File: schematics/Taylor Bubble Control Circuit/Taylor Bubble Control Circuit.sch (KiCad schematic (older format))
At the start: 13 parts, among them J1 Conn_01x01, J2 Conn_01x02, J3 Conn_01x03, U1 L7805CV-DG, U1 STM32F446RE Board, U2 TL062

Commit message: schematics edited
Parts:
- C3, C4: renamed from C?; value C -> 100n
- gave numbers to parts that had none: 2
- renumbered U1 to U2, U2 to U3
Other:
- note added: "3.3V to 4.95V conversion"
- note added: "8... 12 V Voltage Supply Connector\n"
- note added: "ADC input"
- note added: "Transimpedance amplifier"
- note added: "close to U3"
- note removed: "8... 12 V Voltage Supply Input\n"
- note removed: "Analog In"
- note removed: "close to V+"
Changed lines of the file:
@@
 encoding utf-8
 Sheet 1 1
-Title ""
-Date ""
-Rev ""
-Comp ""
+Title "Taylor Bubble Control Circuit"
+Date "2022-07-07"
+Rev "1.0"
+Comp "TU Dresden"
 Comment1 ""
 Comment2 ""
@@
 $EndDescr
 $Comp
-L Amplifier_Operational:TL062 U2
+L Amplifier_Operational:TL062 U3
 U 1 1 62CD608B
 P 2950 2550
-F 0 "U2" H 2950 2917 50  0000 C CNN
+F 0 "U3" H 2950 2917 50  0000 C CNN
 F 1 "TL062" H 2950 2826 50  0000 C CNN
 F 2 "" H 2950 2550 50  0001 C CNN
@@
 $EndComp
 $Comp
-L Amplifier_Operational:TL062 U2
+L Amplifier_Operational:TL062 U3
 U 3 1 62CDCC37
 P 5650 1650
-F 0 "U2" H 5608 1696 50  0000 L CNN
+F 0 "U3" H 5608 1696 50  0000 L CNN
 F 1 "TL062" H 5608 1605 50  0000 L CNN
 F 2 "" H 5650 1650 50  0001 C CNN
@@
 $EndComp
 $Comp
-L Device:R_POT RV?
+L Device:R_POT RV1
 U 1 1 62CF5B88
 P 3450 2800
-F 0 "RV?" V 3335 2800 50  0000 C CNN
+F 0 "RV1" V 3335 2800 50  0000 C CNN
 F 1 "R_POT" V 3244 2800 50  0000 C CNN
 F 2 "" H 3450 2800 50  0001 C CNN
@@
 	2650 2800 2650 2650
 $Comp
-L power:GND #PWR?
+L power:GND #PWR01
 U 1 1 62CF9495
 P 2500 2450
-F 0 "#PWR?" H 2500 2200 50  0001 C CNN
+F 0 "#PWR01" H 2500 2200 50  0001 C CNN
 F 1 "GND" H 2505 2277 50  0000 C CNN
 F 2 "" H 2500 2450 50  0001 C CNN
@@
 	2650 2800 3300 2800
 $Comp
-L power:GND #PWR?
+L power:GND #PWR03
 U 1 1 62D170A5
 P 2650 2900
-F 0 "#PWR?" H 2650 2650 50  0001 C CNN
+F 0 "#PWR03" H 2650 2650 50  0001 C CNN
 F 1 "GND" H 2655 2727 50  0000 C CNN
 F 2 "" H 2650 2900 50  0001 C CNN
@@
 $EndComp
 $Comp
-L Regulator_Linear:L7805 U1
+L Regulator_Linear:L7805 U2
 U 1 1 62D18C8D
 P 3350 1350
-F 0 "U1" H 3350 1592 50  0000 C CNN
+F 0 "U2" H 3350 1592 50  0000 C CNN
 F 1 "L7805CV-DG" H 3350 1501 50  0000 C CNN
 F 2 "" H 3375 1200 50  0001 L CIN
@@
 $EndComp
 $Comp
-L Device:CP C?
+L Device:CP C2
 U 1 1 62D1B42A
 P 3750 1500
-F 0 "C?" H 3868 1546 50  0000 L CNN
+F 0 "C2" H 3868 1546 50  0000 L CNN
 F 1 "330n" H 3868 1455 50  0000 L CNN
 F 2 "" H 3788 1350 50  0001 C CNN
@@
 	3050 1350 2750 1350
 $Comp
-L power:GND #PWR?
+L power:GND #PWR04
 U 1 1 62D1D949
 P 2750 1650
-F 0 "#PWR?" H 2750 1400 50  0001 C CNN
+F 0 "#PWR04" H 2750 1400 50  0001 C CNN
 F 1 "GND" H 2755 1477 50  0000 C CNN
 F 2 "" H 2750 1650 50  0001 C CNN
@@
 $EndComp
 $Comp
-L power:GND #PWR?
+L power:GND #PWR06
 U 1 1 62D1DB97
 P 3750 1650
-F 0 "#PWR?" H 3750 1400 50  0001 C CNN
+F 0 "#PWR06" H 3750 1400 50  0001 C CNN
 F 1 "GND" H 3755 1477 50  0000 C CNN
 F 2 "" H 3750 1650 50  0001 C CNN
@@
 $EndComp
 $Comp
-L power:GND #PWR?
+L power:GND #PWR05
 U 1 1 62D1E0D5
 P 3350 1650
-F 0 "#PWR?" H 3350 1400 50  0001 C CNN
+F 0 "#PWR05" H 3350 1400 50  0001 C CNN
 F 1 "GND" H 3355 1477 50  0000 C CNN
 F 2 "" H 3350 1650 50  0001 C CNN
@@
 Connection ~ 2750 1350
 $Comp
-L power:GND #PWR?
+L power:GND #PWR010
 U 1 1 62D27363
 P 5550 1950
-F 0 "#PWR?" H 5550 1700 50  0001 C CNN
+F 0 "#PWR010" H 5550 1700 50  0001 C CNN
 F 1 "GND" H 5555 1777 50  0000 C CNN
 F 2 "" H 5550 1950 50  0001 C CNN
@@
 close to U1
 $Comp
-L Device:C C?
+L Device:C C4
 U 1 1 62D4D672
 P 5150 1500
-F 0 "C?" H 5035 1454 50  0000 R CNN
-F 1 "C" H 5035 1545 50  0000 R CNN
+F 0 "C4" H 5035 1454 50  0000 R CNN
+F 1 "100n" H 5035 1545 50  0000 R CNN
 F 2 "" H 5188 1350 50  0001 C CNN
 F 3 "~" H 5150 1500 50  0001 C CNN
@@
 $EndComp
 $Comp
-L power:GND #PWR?
+L power:GND #PWR09
 U 1 1 62D4E897
 P 5150 1650
-F 0 "#PWR?" H 5150 1400 50  0001 C CNN
+F 0 "#PWR09" H 5150 1400 50  0001 C CNN
 F 1 "GND" H 5155 1477 50  0000 C CNN
 F 2 "" H 5150 1650 50  0001 C CNN
@@
 $EndComp
 Text Notes 4950 1650 0    50   ~ 0
-close to V+
+close to U3
 Wire Wire Line
 	5150 1350 5550 1350
@@
 	3950 3900 4100 3900
 $Comp
-L power:GND #PWR?
+L power:GND #PWR07
 U 1 1 62DDF2C7
 P 4100 4200
-F 0 "#PWR?" H 4100 3950 50  0001 C CNN
+F 0 "#PWR07" H 4100 3950 50  0001 C CNN
 F 1 "GND" H 4105 4027 50  0000 C CNN
 F 2 "" H 4100 4200 50  0001 C CNN
@@
 $EndComp
 $Comp
-L Device:C C?
+L Device:C C3
 U 1 1 62DDF2C1
 P 4100 4050
-F 0 "C?" H 3985 4004 50  0000 R CNN
-F 1 "C" H 3985 4095 50  0000 R CNN
+F 0 "C3" H 3985 4004 50  0000 R CNN
+F 1 "100n" H 3985 4095 50  0000 R CNN
 F 2 "" H 4138 3900 50  0001 C CNN
 F 3 "~" H 4100 4050 50  0001 C CNN
@@
 	2600 3900 2600 4100
 $Comp
-L Amplifier_Operational:TL062 U2
+L Amplifier_Operational:TL062 U3
 U 2 1 62CE49AF
 P 2900 3800
-F 0 "U2" H 2900 4167 50  0000 C CNN
+F 0 "U3" H 2900 4167 50  0000 C CNN
 F 1 "TL062" H 2900 4076 50  0000 C CNN
 F 2 "" H 2900 3800 50  0001 C CNN
@@
 	3200 4100 2600 4100
 $Comp
-L power:GND #PWR?
+L power:GND #PWR02
 U 1 1 62D6259C
 P 2600 4500
-F 0 "#PWR?" H 2600 4250 50  0001 C CNN
+F 0 "#PWR02" H 2600 4250 50  0001 C CNN
 F 1 "GND" H 2605 4327 50  0000 C CNN
 F 2 "" H 2600 4500 50  0001 C CNN
@@
 Servo Motor Connectors
 $Comp
-L power:GND #PWR?
+L power:GND #PWR08
 U 1 1 62DDD2CF
 P 4600 4000
-F 0 "#PWR?" H 4600 3750 50  0001 C CNN
+F 0 "#PWR08" H 4600 3750 50  0001 C CNN
 F 1 "GND" H 4605 3827 50  0000 C CNN
 F 2 "" H 4600 4000 50  0001 C CNN
@@
 Wire Notes Line
 	1400 1500 1400 1200
-Text Notes 1250 1150 0    50   ~ 0
-8... 12 V Voltage Supply Input\n
 Wire Wire Line
 	1950 2800 2650 2800
@@
 PWM_3v3
 Text Notes 9400 1550 0    50   ~ 0
-Analog In
+ADC input
 Text GLabel 9850 1550 2    50   Input ~ 0
 PhotoVoltage
@@
 	8650 4850 8650 4800
 $Comp
-L power:GND #PWR?
+L power:GND #PWR011
 U 1 1 62D8D228
 P 8650 4850
-F 0 "#PWR?" H 8650 4600 50  0001 C CNN
+F 0 "#PWR011" H 8650 4600 50  0001 C CNN
 F 1 "GND" H 8650 4700 50  0000 C CNN
 F 2 "" H 8650 4850 50  0001 C CNN
@@
 NoConn ~ 9350 1750
 NoConn ~ 9350 1850
+Text Notes 2550 1650 0    50   ~ 0
+close to U1
+Text Notes 2550 2100 0    50   ~ 0
+Transimpedance amplifier
+Text Notes 2500 3350 0    50   ~ 0
+3.3V to 4.95V conversion
+Text Notes 1250 1150 0    50   ~ 0
+8... 12 V Voltage Supply Connector\n
 $EndSCHEMATC

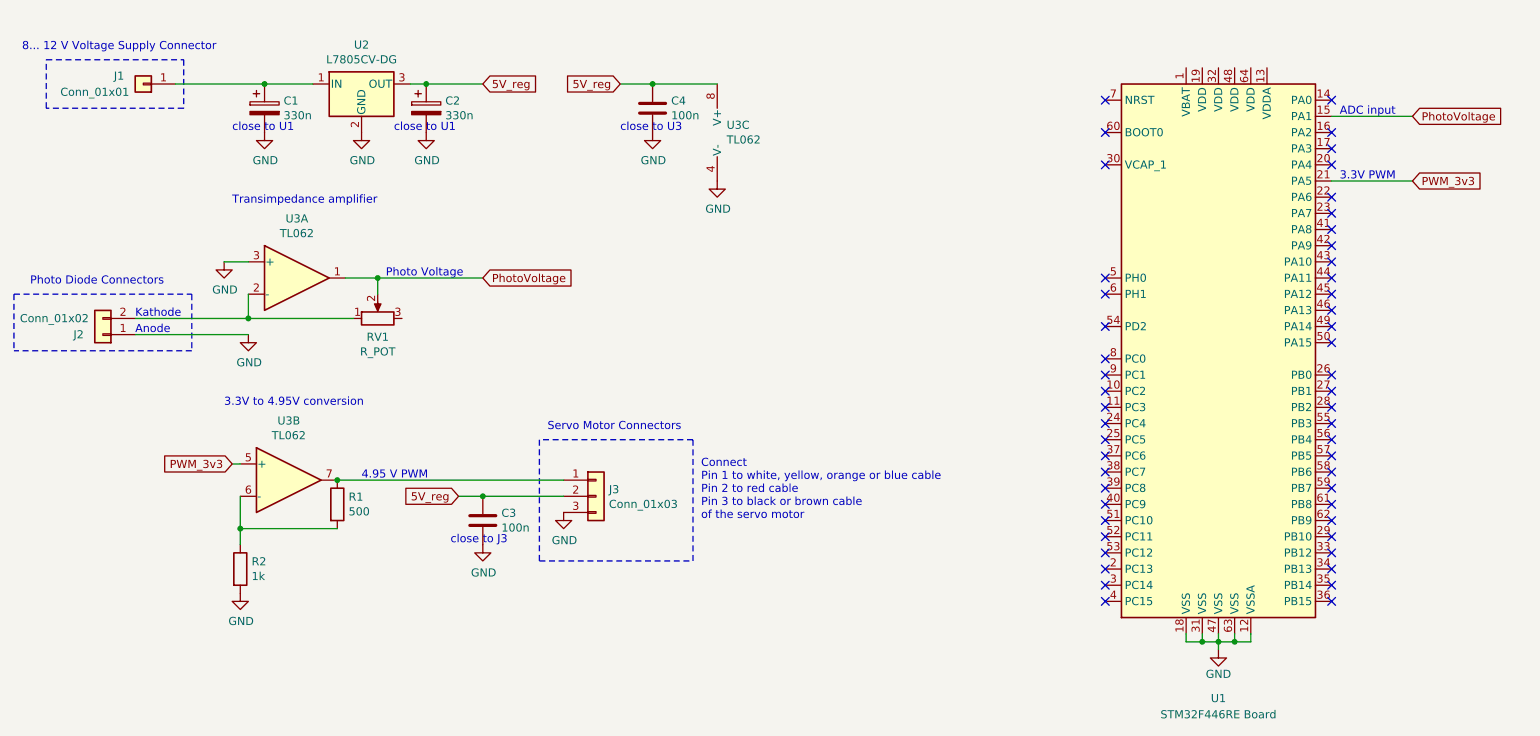
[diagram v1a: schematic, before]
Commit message: updated schematics
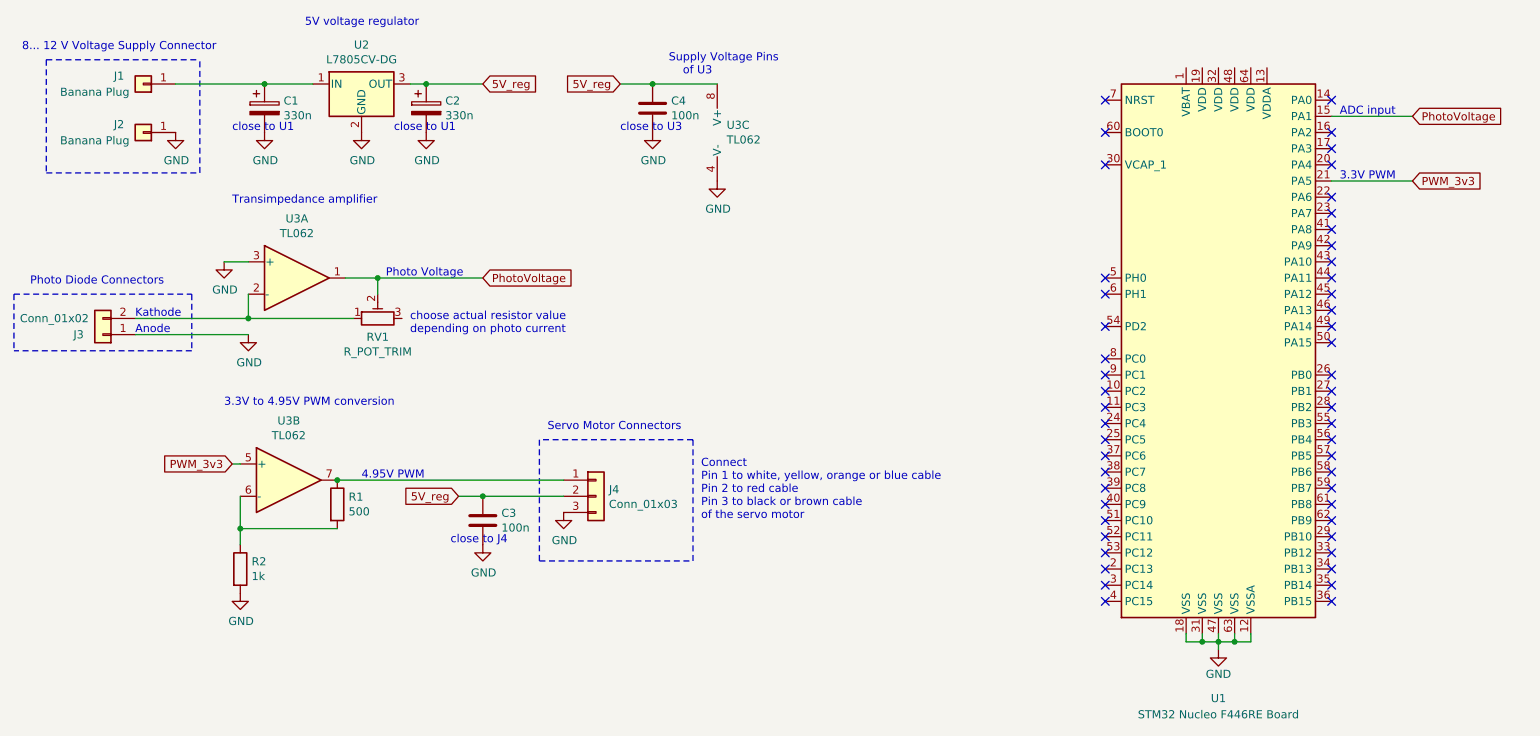
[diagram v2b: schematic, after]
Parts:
- removed RV1: R_POT, symbol Device:R_POT
- added J2: Banana Plug, symbol Connector_Generic:Conn_01x01
- added RV1: R_POT_TRIM, symbol Device:R_POT_TRIM
- C1, C2: Reichelt link (none) -> https://www.reichelt.de/subminiatur-elko-radial-330-nf-63-v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
- C3, C4: Reichelt link (none) -> https://www.reichelt.de/keramik-kondensator-100-nf-20-80-y5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
- J1: value Conn_01x01 -> Banana Plug; Reichelt link (none) -> https://www.reichelt.de/bananenbuchse-4mm-vollisoliert-rot-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
- J3: renamed from J2; Reichelt link (none) -> https://www.reichelt.de/fahrstuhlklemme-2-pol-4-mm-rm-5-08-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
- J4: renamed from J3; Reichelt link (none) -> https://www.reichelt.de/fahrstuhlklemme-3-pol-4-mm-rm-5-08-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
- U1: value STM32F446RE Board -> STM32 Nucleo F446RE Board; Reichelt link (none) -> https://www.reichelt.de/nucleo-64-arm-cortex-stm32-f446-ser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
- U2: Reichelt link (none) -> https://www.reichelt.de/spannungsregler-fest-5-v-1-5a-4-to-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
- U3: Reichelt link (none) -> https://www.reichelt.de/operationsverstaerker-2-fach-dip-8-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
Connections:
- net GND: now also J2.1 (Pin_1)
- net PhotoVoltage: now also RV1.2
- net at J3.2 (Pin_2), U3.2 (-): now also RV1.1
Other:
- note added: "3.3V to 4.95V PWM conversion"
- note added: "4.95V PWM"
- note added: "5V voltage regulator"
- note added: "Supply Voltage Pins \n of U3"
- note added: "choose actual resistor value \ndepending on photo current"
- note added: "close to J4"
- note removed: "3.3V to 4.95V conversion"
- note removed: "4.95 V PWM"
- note removed: "close to J3"
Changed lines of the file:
@@
 F 1 "TL062" H 2950 2826 50  0000 C CNN
 F 2 "" H 2950 2550 50  0001 C CNN
-F 3 "http://www.ti.com/lit/ds/symlink/tl061.pdf" H 2950 2550 50  0001 C CNN
+F 3 "https://www.reichelt.de/index.html?ACTION=7&LA=3&OPEN=0&INDEX=0&FILENAME=A200%2FTL062%23STM.pdf" H 2950 2550 50  0001 C CNN
+F 4 "https://www.reichelt.de/operationsverstaerker-2-fach-dip-8-tl-062-dip-p21552.html?&GROUP=A2C4&START=0&SORT=preis&OFFSET=16&nbc=1" H 2950 2550 50  0001 C CNN "Reichelt link"
 	1    2950 2550
 	1    0    0    -1
@@
 F 1 "TL062" H 5608 1605 50  0000 L CNN
 F 2 "" H 5650 1650 50  0001 C CNN
-F 3 "http://www.ti.com/lit/ds/symlink/tl061.pdf" H 5650 1650 50  0001 C CNN
+F 3 "https://www.reichelt.de/index.html?ACTION=7&LA=3&OPEN=0&INDEX=0&FILENAME=A200%2FTL062%23STM.pdf" H 5650 1650 50  0001 C CNN
+F 4 "https://www.reichelt.de/operationsverstaerker-2-fach-dip-8-tl-062-dip-p21552.html?&GROUP=A2C4&START=0&SORT=preis&OFFSET=16&nbc=1" H 5650 1650 50  0001 C CNN "Reichelt link"
 	3    5650 1650
 	1    0    0    -1
-$EndComp
-$Comp
-L Device:R_POT RV1
-U 1 1 62CF5B88
-P 3450 2800
-F 0 "RV1" V 3335 2800 50  0000 C CNN
-F 1 "R_POT" V 3244 2800 50  0000 C CNN
-F 2 "" H 3450 2800 50  0001 C CNN
-F 3 "~" H 3450 2800 50  0001 C CNN
-	1    3450 2800
-	0    -1   -1   0
 $EndComp
 Wire Wire Line
@@
 F 1 "L7805CV-DG" H 3350 1501 50  0000 C CNN
 F 2 "" H 3375 1200 50  0001 L CIN
-F 3 "http://www.st.com/content/ccc/resource/technical/document/datasheet/41/4f/b3/b0/12/d4/47/88/CD00000444.pdf/files/CD00000444.pdf/jcr:content/translations/en.CD00000444.pdf" H 3350 1300 50  0001 C CNN
+F 3 "https://www.reichelt.de/index.html?ACTION=7&LA=3&OPEN=0&INDEX=0&FILENAME=A200%2FL78_ENG_TDS.pdf" H 3350 1300 50  0001 C CNN
+F 4 "https://www.reichelt.de/spannungsregler-fest-5-v-1-5a-4-to-220-l7805cv-dg-stm-p216677.html?&GROUP=A2A2&START=0&SORT=preis&OFFSET=16&nbc=1" H 3350 1350 50  0001 C CNN "Reichelt link"
 	1    3350 1350
 	1    0    0    -1
@@
 F 1 "330n" H 2868 1455 50  0000 L CNN
 F 2 "" H 2788 1350 50  0001 C CNN
-F 3 "~" H 2750 1500 50  0001 C CNN
+F 3 "https://www.reichelt.de/index.html?ACTION=7&LA=3&OPEN=0&INDEX=0&FILENAME=B300%2FSM_TRANS.pdf" H 2750 1500 50  0001 C CNN
+F 4 "https://www.reichelt.de/subminiatur-elko-radial-330-nf-63-v-rm-1-5-85-c-1000h-20--sm-0-33-63rad-p18159.html?&GROUP=B315&START=0&SORT=preis&OFFSET=16&nbc=1" H 2750 1500 50  0001 C CNN "Reichelt link"
 	1    2750 1500
 	1    0    0    -1
@@
 F 1 "330n" H 3868 1455 50  0000 L CNN
 F 2 "" H 3788 1350 50  0001 C CNN
-F 3 "~" H 3750 1500 50  0001 C CNN
+F 3 "https://www.reichelt.de/index.html?ACTION=7&LA=3&OPEN=0&INDEX=0&FILENAME=B300%2FSM_TRANS.pdf" H 3750 1500 50  0001 C CNN
+F 4 "https://www.reichelt.de/subminiatur-elko-radial-330-nf-63-v-rm-1-5-85-c-1000h-20--sm-0-33-63rad-p18159.html?&GROUP=B315&START=0&SORT=preis&OFFSET=16&nbc=1" H 3750 1500 50  0001 C CNN "Reichelt link"
 	1    3750 1500
 	1    0    0    -1
@@
 F 1 "100n" H 5035 1545 50  0000 R CNN
 F 2 "" H 5188 1350 50  0001 C CNN
-F 3 "~" H 5150 1500 50  0001 C CNN
+F 3 "https://www.reichelt.de/index.html?ACTION=7&LA=3&OPEN=0&INDEX=0&FILENAME=B300%2Fkerko.pdf" H 5150 1500 50  0001 C CNN
+F 4 "https://www.reichelt.de/keramik-kondensator-100-nf-20-80-y5v-50-100-v-rm-5-kerko-100n-p9265.html?&GROUP=B353&START=0&SORT=preis&OFFSET=16&nbc=1" H 5150 1500 50  0001 C CNN "Reichelt link"
 	1    5150 1500
 	-1   0    0    1
@@
 P 2000 1350
 F 0 "J1" H 2150 1300 50  0000 C CNN
-F 1 "Conn_01x01" H 2300 1400 50  0000 C CNN
+F 1 "Banana Plug" H 2300 1400 50  0000 C CNN
 F 2 "" H 2000 1350 50  0001 C CNN
 F 3 "~" H 2000 1350 50  0001 C CNN
+F 4 "https://www.reichelt.de/bananenbuchse-4mm-vollisoliert-rot-bb-4-rt-p4896.html?&trstct=pos_9&nbc=1" H 2000 1350 50  0001 C CNN "Reichelt link"
 	1    2000 1350
 	-1   0    0    1
@@
 F 1 "100n" H 3985 4095 50  0000 R CNN
 F 2 "" H 4138 3900 50  0001 C CNN
-F 3 "~" H 4100 4050 50  0001 C CNN
+F 3 "https://www.reichelt.de/index.html?ACTION=7&LA=3&OPEN=0&INDEX=0&FILENAME=B300%2Fkerko.pdf" H 4100 4050 50  0001 C CNN
+F 4 "https://www.reichelt.de/keramik-kondensator-100-nf-20-80-y5v-50-100-v-rm-5-kerko-100n-p9265.html?&GROUP=B353&START=0&SORT=preis&OFFSET=16&nbc=1" H 4100 4050 50  0001 C CNN "Reichelt link"
 	1    4100 4050
 	-1   0    0    1
@@
 F 1 "TL062" H 2900 4076 50  0000 C CNN
 F 2 "" H 2900 3800 50  0001 C CNN
-F 3 "http://www.ti.com/lit/ds/symlink/tl061.pdf" H 2900 3800 50  0001 C CNN
+F 3 "https://www.reichelt.de/index.html?ACTION=7&LA=3&OPEN=0&INDEX=0&FILENAME=A200%2FTL062%23STM.pdf" H 2900 3800 50  0001 C CNN
+F 4 "https://www.reichelt.de/operationsverstaerker-2-fach-dip-8-tl-062-dip-p21552.html?&GROUP=A2C4&START=0&SORT=preis&OFFSET=16&nbc=1" H 2900 3800 50  0001 C CNN "Reichelt link"
 	2    2900 3800
 	1    0    0    -1
@@
 $EndComp
 $Comp
-L Connector_Generic:Conn_01x03 J3
+L Connector_Generic:Conn_01x03 J4
 U 1 1 62D238DB
 P 4800 3900
-F 0 "J3" H 4880 3942 50  0000 L CNN
+F 0 "J4" H 4880 3942 50  0000 L CNN
 F 1 "Conn_01x03" H 4880 3851 50  0000 L CNN
 F 2 "" H 4800 3900 50  0001 C CNN
 F 3 "~" H 4800 3900 50  0001 C CNN
+F 4 "https://www.reichelt.de/fahrstuhlklemme-3-pol-4-mm-rm-5-08-akl-073-03-p36621.html?&GROUP=C1F3&START=0&SORT=preis&OFFSET=16&nbc=1" H 4800 3900 50  0001 C CNN "Reichelt link"
 	1    4800 3900
 	1    0    0    -1
@@
 Connect\nPin 1 to white, yellow, orange or blue cable\nPin 2 to red cable\nPin 3 to black or brown cable\nof the servo motor
 Text Notes 3350 3800 0    50   ~ 0
-4.95 V PWM
+4.95V PWM
 Wire Notes Line
 	4450 3550 4450 4300
@@
 Wire Notes Line
 	5400 3550 4450 3550
-Wire Notes Line
-	1400 1200 2250 1200
-Wire Notes Line
-	2250 1200 2250 1500
-Wire Notes Line
-	2250 1500 1400 1500
-Wire Notes Line
-	1400 1500 1400 1200
 Wire Wire Line
 	1950 2800 2650 2800
@@
 	1200 2650 1200 3000
 $Comp
-L Connector_Generic:Conn_01x02 J2
+L Connector_Generic:Conn_01x02 J3
 U 1 1 62D22E75
 P 1750 2900
-F 0 "J2" H 1900 2900 50  0000 C CNN
+F 0 "J3" H 1900 2900 50  0000 C CNN
 F 1 "Conn_01x02" H 2050 2800 50  0000 C CNN
 F 2 "" H 1750 2900 50  0001 C CNN
 F 3 "~" H 1750 2900 50  0001 C CNN
+F 4 "https://www.reichelt.de/fahrstuhlklemme-2-pol-4-mm-rm-5-08-akl-073-02-p36620.html?&nbc=1&trstct=lsbght_sldr::36621" H 1750 2900 50  0001 C CNN "Reichelt link"
 	1    1750 2900
 	-1   0    0    1
 $EndComp
 Text Notes 3900 4200 0    50   ~ 0
-close to J3
+close to J4
 Wire Wire Line
 	3200 3800 4600 3800
@@
 P 8650 2950
 F 0 "U1" H 8650 750 50  0000 C CNN
-F 1 "STM32F446RE Board" H 8650 650 50  0000 C CNN
+F 1 "STM32 Nucleo F446RE Board" H 8650 650 50  0000 C CNN
 F 2 "Package_QFP:LQFP-64_10x10mm_P0.5mm" H 8050 1250 50  0001 R CNN
-F 3 "http://www.st.com/st-web-ui/static/active/en/resource/technical/document/datasheet/DM00141306.pdf" H 8650 2950 50  0001 C CNN
+F 3 "https://www.st.com/resource/en/user_manual/um1724-stm32-nucleo64-boards-mb1136-stmicroelectronics.pdf" H 8650 2950 50  0001 C CNN
+F 4 "https://www.reichelt.de/nucleo-64-arm-cortex-stm32-f446-serie-nucleo-f446re-p217196.html?search=stm32f446" H 8650 2950 50  0001 C CNN "Reichelt link"
 	1    8650 2950
 	1    0    0    -1
@@
 Transimpedance amplifier
 Text Notes 2500 3350 0    50   ~ 0
-3.3V to 4.95V conversion
+3.3V to 4.95V PWM conversion
 Text Notes 1250 1150 0    50   ~ 0
 8... 12 V Voltage Supply Connector\n
+Text Notes 5250 1300 0    50   ~ 0
+Supply Voltage Pins \n    of U3
+Text Notes 3000 1000 0    50   ~ 0
+5V voltage regulator
+Text Notes 3650 2900 0    50   ~ 0
+choose actual resistor value \ndepending on photo current
+$Comp
+L Device:R_POT_TRIM RV1
+U 1 1 62D00CBC
+P 3450 2800
+F 0 "RV1" V 3335 2800 50  0000 C CNN
+F 1 "R_POT_TRIM" V 3244 2800 50  0000 C CNN
+F 2 "" H 3450 2800 50  0001 C CNN
+F 3 "~" H 3450 2800 50  0001 C CNN
+	1    3450 2800
+	0    -1   -1   0
+$EndComp
+$Comp
+L Connector_Generic:Conn_01x01 J2
+U 1 1 62D04412
+P 2000 1650
+F 0 "J2" H 2150 1600 50  0000 C CNN
+F 1 "Banana Plug" H 2300 1700 50  0000 C CNN
+F 2 "" H 2000 1650 50  0001 C CNN
+F 3 "~" H 2000 1650 50  0001 C CNN
+F 4 "https://www.reichelt.de/bananenbuchse-4mm-vollisoliert-schwarz-bb-4-sw-p4897.html?&trstct=pos_3&nbc=1" H 2000 1650 50  0001 C CNN "Reichelt link"
+	1    2000 1650
+	-1   0    0    1
+$EndComp
+$Comp
+L power:GND #PWR?
+U 1 1 62D04E76
+P 2200 1650
+F 0 "#PWR?" H 2200 1400 50  0001 C CNN
+F 1 "GND" H 2205 1477 50  0000 C CNN
+F 2 "" H 2200 1650 50  0001 C CNN
+F 3 "" H 2200 1650 50  0001 C CNN
+	1    2200 1650
+	1    0    0    -1
+$EndComp
+Wire Notes Line
+	1400 1900 2350 1900
+Wire Notes Line
+	2350 1900 2350 1200
+Wire Notes Line
+	1400 1200 2350 1200
+Wire Notes Line
+	1400 1200 1400 1900
 $EndSCHEMATC

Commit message: edited schematics
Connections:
- net PWM_3v3 renamed PWM_3V3
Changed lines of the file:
@@
 	2550 3700 2600 3700
 Text GLabel 2550 3700 0    50   Input ~ 0
-PWM_3v3
+PWM_3V3
 Wire Wire Line
 	2600 4100 2600 4200
@@
 3.3V PWM
 Text GLabel 9850 1950 2    50   Input ~ 0
-PWM_3v3
+PWM_3V3
 Text Notes 9400 1550 0    50   ~ 0
 ADC input
